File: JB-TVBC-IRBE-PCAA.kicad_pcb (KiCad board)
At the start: 2 copper layers, 35 x 15 mm, 6 parts, among them J1 SJ-435107, J2 SJ-435107

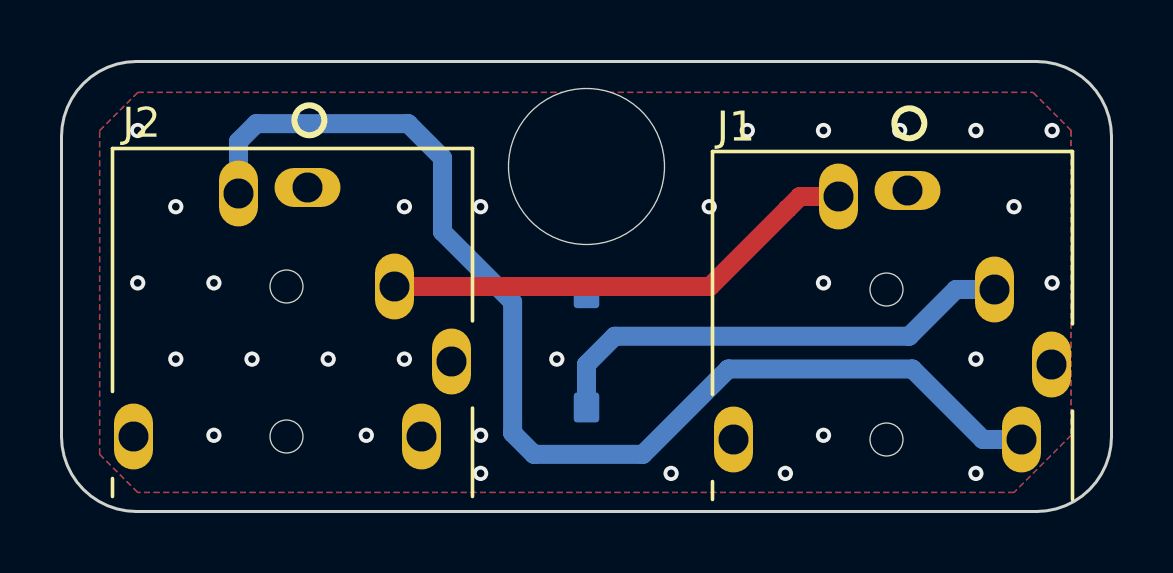
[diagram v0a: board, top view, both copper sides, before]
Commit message: adding text on silkscreen
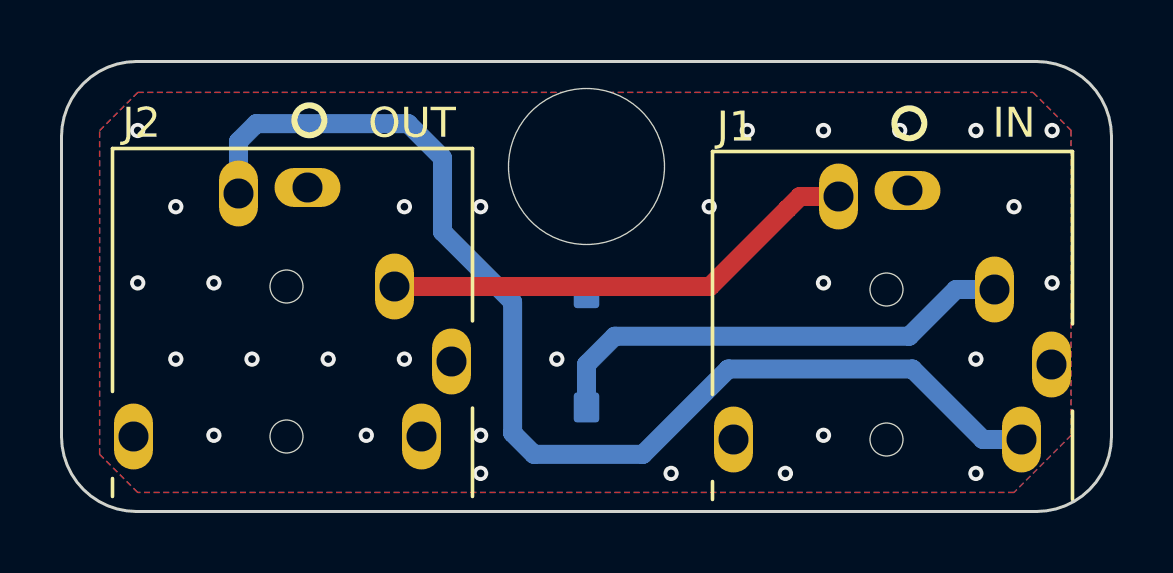
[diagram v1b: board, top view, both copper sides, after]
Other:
- board text added: "IN"
- board text added: "OUT"
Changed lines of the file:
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@@
   (general
     (thickness 1.6)
-    (drawings 11)
+    (drawings 13)
     (tracks 54)
     (zones 0)
@@
     )
   )
+  (gr_text OUT (at 111.684 97.046) (layer F.SilkS)
+    (effects (font (size 1 1) (thickness 0.15)))
+  )
+  (gr_text IN (at 131.75 97.046) (layer F.SilkS)
+    (effects (font (size 1 1) (thickness 0.15)))
+  )
   (gr_poly (pts (xy 130.099 106.19) (xy 123.368 106.19) (xy 123.368 104.031) (xy 130.099 104.031)) (layer B.SilkS) (width 0.1))
